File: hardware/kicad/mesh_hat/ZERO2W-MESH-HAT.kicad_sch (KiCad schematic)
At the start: 0 parts

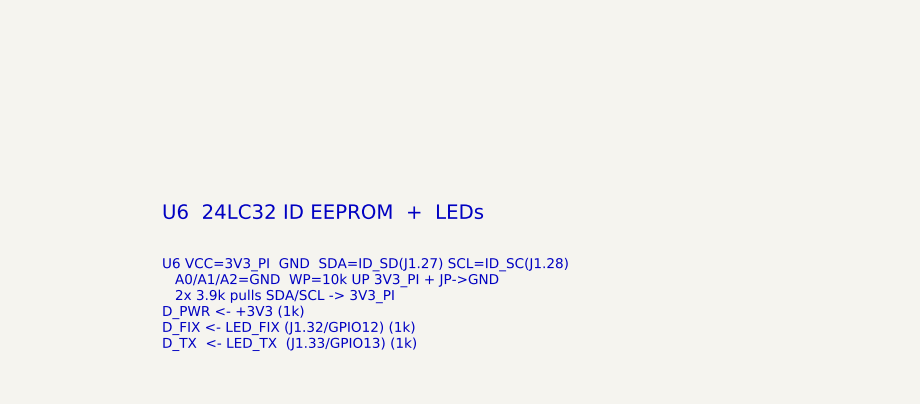
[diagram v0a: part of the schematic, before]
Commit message: Add grounding/shield/routing plan; roll shields into schematic + BOM
- docs/MESH_HAT_GROUNDING.md: ground via-stitching plan (RF fence <=3mm,
  edge ring, plane stitch grid, module pad array, 900MHz<->GNSS moat),
  optional DNP RF shield cans (MM8108 module is pre-shielded), and the
  layer-by-layer routing order (RF first, then USB pair, GND pour, power,
  digital, stitch, DRC).
- BOM: add SH1 (GNSS, Wuerth 20x20) + SH2 (MM8108, Laird BMI-S-209-F),
  both DNP, frame pins -> GND.
- Schematic doc + KiCad scaffold: reference SH1/SH2 -> GND. Scaffold
  regenerated and validated.

https://claude.ai/code/session_015nkkW85U3sPf5mcvrsMw7T
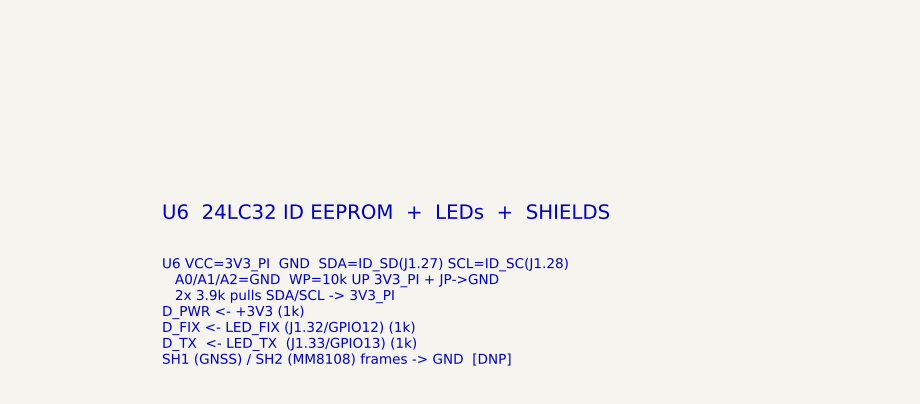
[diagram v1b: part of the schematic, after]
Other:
- note added: "U6 24LC32 ID EEPROM + LEDs + SHIELDS"
- note added: "U6 VCC=3V3_PI GND SDA=ID_SD(J1.27) SCL=ID_SC(J1.28) A0/A1/A2=GND WP=10k UP 3V3_PI + JP->GND 2x 3.9k pulls SDA/SCL -> 3V3_PI D_PWR <- +3V3 (1k) D_FIX <- LED_FIX (J1.32/GPIO12) (1k) D_TX <- LED_TX (J1.33/GPIO13) (1k) SH1 (GNSS) / SH2 (MM8108) frames -> GND [DNP]"
- note removed: "U6 24LC32 ID EEPROM + LEDs"
- note removed: "U6 VCC=3V3_PI GND SDA=ID_SD(J1.27) SCL=ID_SC(J1.28) A0/A1/A2=GND WP=10k UP 3V3_PI + JP->GND 2x 3.9k pulls SDA/SCL -> 3V3_PI D_PWR <- +3V3 (1k) D_FIX <- LED_FIX (J1.32/GPIO12) (1k) D_TX <- LED_TX (J1.33/GPIO13) (1k)"
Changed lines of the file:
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@@
 	(text "USB-C ETHERNET PASS-THROUGH (no hub)" (exclude_from_sim no) (at 25 140 0) (effects (font (size 1.6 1.6) (thickness 0.25)) (justify left top)))
 	(text "Pi USB host -> cable -> J7 -> board -> J6 -> dongle\nJ7 MicroB D+/D- -> USB_DP/USB_DM ; GND ; VBUS/ID NC\nD1 USBLC6-2 ESD on USB_DP/USB_DM\nJ6 USB-C D+(A6,B6)->USB_DP  D-(A7,B7)->USB_DM\nJ6 VBUS(A4/B4/A9/B9) -> VBUS_C\nJ6 CC1->56k->VBUS_C  CC2->56k->VBUS_C (Rp host)\nU11 FPF2123: IN=+5V OUT=VBUS_C EN=on ILIM~0.5-1A\nPi: dtoverlay=dwc2,dr_mode=host ; OTG cable" (exclude_from_sim no) (at 25 146 0) (effects (font (size 1.1 1.1)) (justify left top)))
-	(text "U6  24LC32 ID EEPROM  +  LEDs" (exclude_from_sim no) (at 170 140 0) (effects (font (size 1.6 1.6) (thickness 0.25)) (justify left top)))
-	(text "U6 VCC=3V3_PI  GND  SDA=ID_SD(J1.27) SCL=ID_SC(J1.28)\n   A0/A1/A2=GND  WP=10k UP 3V3_PI + JP->GND\n   2x 3.9k pulls SDA/SCL -> 3V3_PI\nD_PWR <- +3V3 (1k)\nD_FIX <- LED_FIX (J1.32/GPIO12) (1k)\nD_TX  <- LED_TX  (J1.33/GPIO13) (1k)" (exclude_from_sim no) (at 170 146 0) (effects (font (size 1.1 1.1)) (justify left top)))
+	(text "U6  24LC32 ID EEPROM  +  LEDs  +  SHIELDS" (exclude_from_sim no) (at 170 140 0) (effects (font (size 1.6 1.6) (thickness 0.25)) (justify left top)))
+	(text "U6 VCC=3V3_PI  GND  SDA=ID_SD(J1.27) SCL=ID_SC(J1.28)\n   A0/A1/A2=GND  WP=10k UP 3V3_PI + JP->GND\n   2x 3.9k pulls SDA/SCL -> 3V3_PI\nD_PWR <- +3V3 (1k)\nD_FIX <- LED_FIX (J1.32/GPIO12) (1k)\nD_TX  <- LED_TX  (J1.33/GPIO13) (1k)\nSH1 (GNSS) / SH2 (MM8108) frames -> GND  [DNP]" (exclude_from_sim no) (at 170 146 0) (effects (font (size 1.1 1.1)) (justify left top)))
 	(text "J1  Pi 40-pin header (key pins)" (exclude_from_sim no) (at 320 140 0) (effects (font (size 1.6 1.6) (thickness 0.25)) (justify left top)))
 	(text "1,17 3V3_PI   2,4 +5V   GND:6/9/14/20/25/30/34/39\nSPI0: 19 MOSI 21 MISO 23 SCLK 24 CE0/CS\n29 GPIO5 IRQ  11 GPIO17 RST  16 GPIO23 PWR1  18 GPIO24 PWR2\nUART0: 8 TXD0  10 RXD0   12 GPIO18 PPS\nI2C1: 3 SDA  5 SCL   13 GPIO27 GNSS_RST  15 GPIO22 EXTINT\n27 ID_SD  28 ID_SC   32 GPIO12 LED_FIX  33 GPIO13 LED_TX" (exclude_from_sim no) (at 320 146 0) (effects (font (size 1.1 1.1)) (justify left top)))
